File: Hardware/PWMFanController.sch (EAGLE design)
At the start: 9 parts, among them IC1 HT7333, U1 ATtiny85

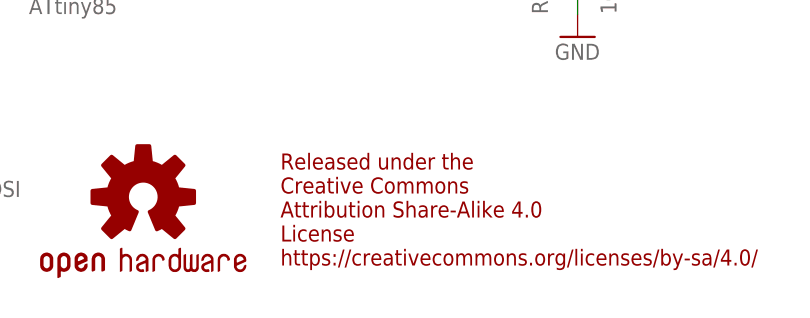
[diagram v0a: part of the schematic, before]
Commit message: Add author mention
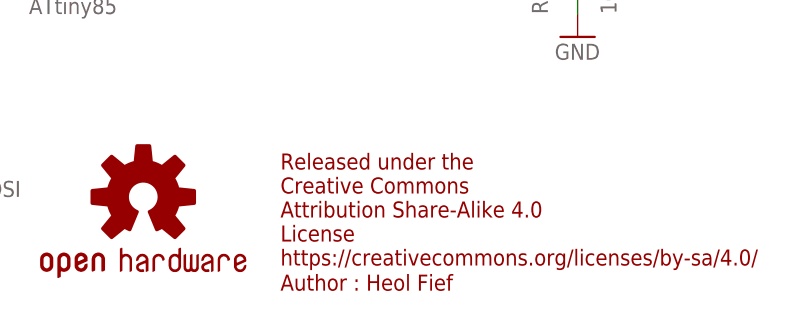
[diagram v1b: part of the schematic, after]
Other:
- note added: "Author : Heol Fief"
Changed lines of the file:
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@@
 <?xml version="1.0" encoding="utf-8"?>
 <!DOCTYPE eagle SYSTEM "eagle.dtd">
-<eagle version="8.2.2">
+<eagle version="8.3.1">
 <drawing>
 <settings>
 <setting alwaysvectorfont="no"/>
+<setting keepoldvectorfont="yes"/>
 <setting verticaltext="up"/>
 </settings>
@@
 License
 https://creativecommons.org/licenses/by-sa/4.0/</text>
+<text x="81.28" y="-0.254" size="1.778" layer="94">Author : Heol Fief</text>
 </plain>
 <instances>
@@
 </note>
 <note version="8.2" severity="warning">
-Since Version 8.2, Eagle supports online libraries. The ids
+Since Version 8.2, EAGLE supports online libraries. The ids
 of those online libraries will not be understood (or retained)
 with this version.
